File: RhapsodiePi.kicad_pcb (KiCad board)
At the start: 2 copper layers, 119 parts, among them J1 Micro_SD_Card_Det, J2 USB_A_Stacked, J3 USB_A_Stacked, J5 RJ45_HR913550A, U1 MT3420C-mt3420c, U1 X1000, U10 TPS65185RGZR, U2 MT3420C-mt3420c, U3 MT3420C-mt3420c, U5 AP6212, U6 FE2.1, U7 RTL8201F, U8 M25PX32-VMW, U9 TFP410PAP, X1 SG-3030CM

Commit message: Update (Display)
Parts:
- removed the U1 at (29.1, 35.7)
- removed the U1 at (111.4, 89.4)
- added C84: 22µ, Capacitor_SMD:C_0603_1608Metric, F.Cu at (43.2, 31.1)
- added C91: 4µ7, Capacitor_SMD:C_0805_2012Metric, F.Cu at (39.0, 33.5)
- added D10: LED, LED_SMD:LED_0402_1005Metric, F.Cu at (152.4, 76.2)
- added D12: LED, LED_SMD:LED_0402_1005Metric, F.Cu at (152.4, 78.6)
- added D13: LED, LED_SMD:LED_0402_1005Metric, F.Cu at (152.4, 81.0)
- added D4: LED, LED_SMD:LED_0402_1005Metric, F.Cu at (152.4, 69.0)
- added D6: LED, LED_SMD:LED_0402_1005Metric, F.Cu at (152.4, 71.4)
- added D8: LED, LED_SMD:LED_0402_1005Metric, F.Cu at (152.4, 73.8)
- added L4: 2µ2, Inductor_SMD:L_1008_2520Metric, F.Cu at (39.1, 25.6)
- added L5: 4µ7, Inductor_SMD:L_1008_2520Metric, F.Cu at (33.6, 30.9)
- added R1: 50K, Resistor_SMD:R_0402_1005Metric, F.Cu at (108.4, 34.2)
- added R14: 100K, Resistor_SMD:R_0402_1005Metric, F.Cu at (144.2, 40.4)
- added R17: 1K, Resistor_SMD:R_0402_1005Metric, F.Cu at (147.1, 38.4)
- added R18: 1K, Resistor_SMD:R_0402_1005Metric, F.Cu at (150.0, 38.4)
- added R19: 1K, Resistor_SMD:R_0402_1005Metric, F.Cu at (152.4, 67.8)
- added R2: 30K, Resistor_SMD:R_0402_1005Metric, F.Cu at (111.3, 36.2)
- added R20: 1K, Resistor_SMD:R_0402_1005Metric, F.Cu at (152.4, 70.2)
- added R21: 1K, Resistor_SMD:R_0402_1005Metric, F.Cu at (152.4, 72.6)
- added R22: 1K, Resistor_SMD:R_0402_1005Metric, F.Cu at (152.4, 75.0)
- added R23: 1K, Resistor_SMD:R_0402_1005Metric, F.Cu at (152.4, 77.4)
- added R24: 1K, Resistor_SMD:R_0402_1005Metric, F.Cu at (152.4, 79.8)
- added R26: 1K, Resistor_SMD:R_0402_1005Metric, F.Cu at (111.3, 41.7)
- added R27: 100K, Resistor_SMD:R_0402_1005Metric, F.Cu at (108.4, 43.7)
- added R28: 100K, Resistor_SMD:R_0402_1005Metric, F.Cu at (114.2, 43.7)
- added R29: 1K, Resistor_SMD:R_0402_1005Metric, F.Cu at (111.3, 43.7)
- added R3: 450K, Resistor_SMD:R_0402_1005Metric, F.Cu at (111.3, 32.2)
- added R30: 100K, Resistor_SMD:R_0402_1005Metric, F.Cu at (114.2, 41.7)
- added R31: 1K, Resistor_SMD:R_0402_1005Metric, F.Cu at (108.4, 41.7)
- added R32: 1K, Resistor_SMD:R_0402_1005Metric, F.Cu at (120.8, 41.7)
- added R33: 1K, Resistor_SMD:R_0402_1005Metric, F.Cu at (123.7, 41.7)
- added R4: 100K, Resistor_SMD:R_0402_1005Metric, F.Cu at (114.2, 36.2)
- added R5: 200K, Resistor_SMD:R_0402_1005Metric, F.Cu at (108.4, 36.2)
- added R6: 100K, Resistor_SMD:R_0402_1005Metric, F.Cu at (111.3, 34.2)
- added R7: 100K, Resistor_SMD:R_0402_1005Metric, F.Cu at (114.2, 34.2)
- added R8: 100K, Resistor_SMD:R_0402_1005Metric, F.Cu at (108.4, 32.2)
- added R9: 1K, Resistor_SMD:R_0402_1005Metric, F.Cu at (114.2, 32.2)
- added U1: MT3420C-mt3420c, Package_TO_SOT_SMD:SOT-23-6, F.Cu at (23.9, 51.3)
- added U4: X1000, TheBrutzlers_Lib:BGA256C80P16X16_1300X1300X130N, F.Cu at (121.8, 80.4)
- added Y1: 12MHz, Crystal:Crystal_SMD_ECS_CSM3X-2Pin_7.6x4.1mm, F.Cu at (145.2, 74.2)
- C47, C48: value C -> 20p
- C58, C67: value 1µ -> 100n
- C62: value C -> 1µ
- C65: value 100n -> C
- C69: value 100n -> 1µ
- C73: value 22µ -> 100n; footprint Capacitor_SMD:C_0603_1608Metric -> Capacitor_SMD:C_0402_1005Metric
- C74, C78, C85: value 4µ7 -> 22µ; footprint Capacitor_SMD:C_0805_2012Metric -> Capacitor_SMD:C_0603_1608Metric
- C75: value 22µ -> 4µ7; footprint Capacitor_SMD:C_0603_1608Metric -> Capacitor_SMD:C_0805_2012Metric
- C80, C86: value 100n -> 4µ7; footprint Capacitor_SMD:C_0402_1005Metric -> Capacitor_SMD:C_0805_2012Metric
- C81: value 10n -> 100n
- C83: value 4µ7 -> 10n; footprint Capacitor_SMD:C_0805_2012Metric -> Capacitor_SMD:C_0402_1005Metric
- C87: value 4µ7 -> 100n; footprint Capacitor_SMD:C_0805_2012Metric -> Capacitor_SMD:C_0402_1005Metric
- moved U7 103.7 mm to (59.6, 48.3), turned to 0 degrees
- moved C56 93.7 mm to (160.3, 53.2)
- moved C41 93.7 mm to (163.2, 53.2)
- moved C48 93.4 mm to (157.2, 55.2)
- moved C53 93.2 mm to (159.8, 57.2)
- moved C46 92.0 mm to (155.8, 59.1)
- moved C42 90.8 mm to (157.5, 53.2)
- moved C51 89.4 mm to (149.4, 46.3)
- moved C59 88.6 mm to (149.1, 48.2)
- moved C43 87.7 mm to (160.1, 55.2)
- moved C44 87.5 mm to (157.0, 57.2)
- moved C52 85.8 mm to (146.0, 50.2)
- moved C61 83.7 mm to (155.8, 61.1)
- moved C54 83.0 mm to (146.5, 46.3)
- moved C57 82.3 mm to (143.1, 52.2)
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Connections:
- AE1 pad 2: AGND2 -> GND
- C1 pad 2: AGND2 -> GND
- C10 pad 2: AGND2 -> GND
- C11 pad 2: AGND2 -> GND
- C12 pad 2: AGND2 -> GND
- C13 pad 2: AGND2 -> GND
- C14 pad 2: AGND2 -> GND
- C15 pad 2: AGND2 -> GND
- C16 pad 2: AGND2 -> GND
- C17 pad 2: AGND2 -> GND
- C18 pad 2: AGND2 -> GND
- C19 pad 2: AGND2 -> GND
- C2 pad 2: AGND2 -> GND
- C20 pad 2: AGND2 -> GND
- C21 pad 2: AGND2 -> GND
- C22 pad 2: AGND2 -> GND
- C23 pad 2: AGND2 -> GND
- C24 pad 2: AGND2 -> GND
- C25 pad 2: AGND2 -> GND
- C26 pad 2: AGND2 -> GND
- C27 pad 2: AGND2 -> GND
- C28 pad 2: AGND2 -> GND
- C29 pad 2: AGND2 -> GND
- C3 pad 2: AGND2 -> GND
- C30 pad 2: AGND2 -> GND
- C31 pad 2: AGND2 -> GND
- C32 pad 2: AGND2 -> GND
- C33 pad 2: AGND2 -> GND
- C34 pad 2: AGND2 -> GND
- C35 pad 2: AGND2 -> GND
- C36 pad 2: AGND2 -> GND
- C37 pad 2: AGND2 -> GND
- C38 pad 2: AGND2 -> GND
- C39 pad 2: AGND2 -> GND
- C4 pad 2: AGND2 -> GND
- C40 pad 2: AGND2 -> GND
- C41 pad 2: AGND2 -> GND
- C42 pad 2: AGND2 -> GND
- C43 pad 2: AGND2 -> GND
- C44 pad 2: AGND2 -> GND
- C45 pad 2: AGND2 -> GND
- C46 pad 2: AGND2 -> GND
- C47 pad 1: AGND2 -> GND
- C48 pad 1: AGND2 -> GND
- C49 pad 2: AGND2 -> GND
- C5 pad 2: AGND2 -> GND
- C50 pad 2: AGND2 -> GND
- C51 pad 2: AGND2 -> GND
- C52 pad 2: AGND2 -> GND
- C53 pad 2: AGND2 -> GND
- C54 pad 2: AGND2 -> GND
- C55 pad 1: Net-(C44-Pad1) -> GND
- C55 pad 2: AGND2 -> Net-(C55-Pad2)
- C56 pad 1: Net-(C50-Pad1) -> Net-(C44-Pad1)
- C56 pad 2: AGND2 -> GND
- C57 pad 1: Net-(C44-Pad1) -> Net-(C50-Pad1)
- C57 pad 2: AGND2 -> GND
- C58 pad 1: +5V -> Net-(C44-Pad1)
- C58 pad 2: AGND2 -> GND
- C59 pad 2: AGND2 -> GND
- C6 pad 2: AGND2 -> GND
- C60 pad 2: AGND2 -> GND
- C61 pad 2: AGND2 -> GND
- C62 pad 1: AGND2 -> +5V
- C62 pad 2: Net-(C62-Pad2) -> GND
- C63 pad 1: AGND2 -> GND
- C64 pad 1: AGND2 -> GND
- C65 pad 1: Net-(C65-Pad1) -> GND
- C65 pad 2: AGND2 -> Net-(C65-Pad2)
- C66 pad 2: AGND2 -> GND
- C67 pad 1: AGND2 -> Net-(C67-Pad1)
- C67 pad 2: +3V3 -> GND
- C68 pad 1: AGND2 -> GND
- C68 pad 2: Net-(C68-Pad2) -> +3V3
- C69 pad 1: AGND2 -> GND
- C69 pad 2: +3V3 -> Net-(C69-Pad2)
- C7 pad 2: AGND2 -> GND
- C70 pad 1: AGND2 -> GND
- C70 pad 2: Net-(C68-Pad2) -> +3V3
- C71 pad 1: AGND2 -> GND
- C71 pad 2: Net-(C71-Pad2) -> Net-(C69-Pad2)
- C72 pad 1: AGND2 -> GND
- C73 pad 1: unconnected-(C73-Pad1) -> GND
- C73 pad 2: unconnected-(C73-Pad2) -> Net-(C73-Pad2)
- C74 pad 1: AGND2 -> unconnected-(C74-Pad1)
- C74 pad 2: /Display/E-PAPER/VB -> unconnected-(C74-Pad2)
- C75 pad 1: AGND2 -> GND
- C75 pad 2: +5V -> /Display/E-PAPER/VB
- C76 pad 1: +5V -> GND
- C76 pad 2: AGND2 -> +5V
- C77 pad 2: AGND2 -> GND
- C78 pad 1: AGND2 -> +5V
- C78 pad 2: /Display/E-PAPER/VN -> GND
- C79 pad 1: /Display/E-PAPER/VB -> GND
- C79 pad 2: AGND2 -> /Display/E-PAPER/VN
- C8 pad 2: AGND2 -> GND
- C80 pad 1: Net-(C80-Pad1) -> /Display/E-PAPER/VB
- C80 pad 2: AGND2 -> GND
- C81 pad 2: Net-(C81-Pad2) -> GND
- C83 pad 1: AGND2 -> Net-(C83-Pad1)
- C85 pad 1: AGND2 -> Net-(C85-Pad1)
- C85 pad 2: Net-(C85-Pad2) -> GND
- C86 pad 1: Net-(C86-Pad1) -> GND
- C86 pad 2: AGND2 -> Net-(C86-Pad2)
- C87 pad 1: AGND2 -> Net-(C87-Pad1)
- C87 pad 2: Net-(C87-Pad2) -> GND
- C88 pad 1: AGND2 -> GND
- C88 pad 2: /Display/E-PAPER/VEE -> Net-(C88-Pad2)
- C89 pad 1: AGND2 -> GND
- C89 pad 2: /Display/E-PAPER/VDDH -> /Display/E-PAPER/VEE
- C9 pad 2: AGND2 -> GND
- C90 pad 1: /Display/E-PAPER/VN -> GND
- C90 pad 2: AGND2 -> /Display/E-PAPER/VDDH
- D15 pad 1: Net-(C80-Pad1) -> Net-(C81-Pad1)
- D15 pad 2: Net-(C81-Pad2) -> Net-(C82-Pad2)
- D16 pad 1: Net-(C82-Pad2) -> Net-(C83-Pad2)
- D16 pad 2: Net-(C86-Pad1) -> Net-(C87-Pad1)
- D17 pad 1: Net-(C81-Pad2) -> Net-(C82-Pad2)
- D18 pad 2: Net-(C82-Pad2) -> Net-(C83-Pad2)
- FB1 pad 2: Net-(C68-Pad2) -> Net-(C69-Pad2)
- J1 pad 10: AGND2 -> GND
- J1 pad 6: AGND2 -> GND
- J2 pad 4: AGND2 -> GND
- J2 pad 8: AGND2 -> GND
- J2 pad 9: AGND2 -> GND
- J3 pad 4: AGND2 -> GND
- J3 pad 8: AGND2 -> GND
- J3 pad 9: AGND2 -> GND
- J5 pad 2: Net-(C65-Pad1) -> Net-(C66-Pad1)
- J5 pad 5: Net-(C66-Pad1) -> Net-(C67-Pad1)
- J5 pad 8: AGND2 -> GND
- J5 pad SH: AGND2 -> GND
- R13 pad 2: AGND2 -> GND
- R16 pad 1: AGND2 -> GND
- U10 pad 1: Net-(C84-Pad1) -> Net-(C85-Pad1)
- U10 pad 12: unconnected-(U10-Pad12) -> /Display/E-PAPER/XVCOM_CTRL
- U10 pad 15: Net-(C83-Pad2) -> /Display/E-PAPER/VCOM
- U10 pad 17: unconnected-(U10-Pad17) -> /Display/E-PAPER/XSCL
- U10 pad 18: unconnected-(U10-Pad18) -> /Display/E-PAPER/XSDA
- U10 pad 2: unconnected-(U10-Pad2) -> /Display/E-PAPER/X~{INT}
- U10 pad 21: unconnected-(U10-Pad21) -> /Display/E-PAPER/XPWRUP
- U10 pad 23: unconnected-(U10-Pad23) -> /Display/E-PAPER/XPWR_GOOD
- U10 pad 28: Net-(C81-Pad1) -> Net-(C82-Pad1)
- U10 pad 3: Net-(C85-Pad2) -> Net-(C86-Pad2)
- U10 pad 30: Net-(C80-Pad1) -> Net-(C81-Pad1)
- U10 pad 32: AGND2 -> GND
- U10 pad 34: Net-(C86-Pad1) -> Net-(C87-Pad1)
- U10 pad 36: Net-(C82-Pad1) -> Net-(C83-Pad1)
- U10 pad 41: AGND2 -> GND
- U10 pad 44: Net-(C87-Pad2) -> Net-(C88-Pad2)
- U10 pad 46: unconnected-(U10-Pad46) -> /Display/E-PAPER/VDD
- U10 pad 48: AGND2 -> GND
- U10 pad 5: unconnected-(U10-Pad5) -> /Display/E-PAPER/XWAKEU
- U10 pad 6: AGND2 -> GND
- U10 pad 8: AGND2 -> GND
- U2 pad 2: AGND2 -> GND
- U3 pad 2: AGND2 -> GND
- U5 pad 1: AGND2 -> GND
- U5 pad 20: AGND2 -> GND
- U5 pad 3: AGND2 -> GND
- U5 pad 31: AGND2 -> GND
- U5 pad 33: AGND2 -> GND
- U5 pad 36: AGND2 -> GND
- U6 pad 10: AGND2 -> GND
- U6 pad 24: AGND2 -> GND
- U6 pad 39: AGND2 -> GND
- U6 pad 40: Net-(R15-Pad2) -> Net-(C55-Pad2)
- U7 pad 2: Net-(C72-Pad2) -> Net-(C73-Pad2)
- U7 pad 29: Net-(C71-Pad2) -> Net-(C72-Pad2)
- U7 pad 30: Net-(C68-Pad2) -> Net-(C69-Pad2)
- U7 pad 33: AGND2 -> GND
- U7 pad 7: Net-(C68-Pad2) -> Net-(C69-Pad2)
- U8 pad 4: AGND2 -> GND
- X1 pad 2: AGND2 -> GND

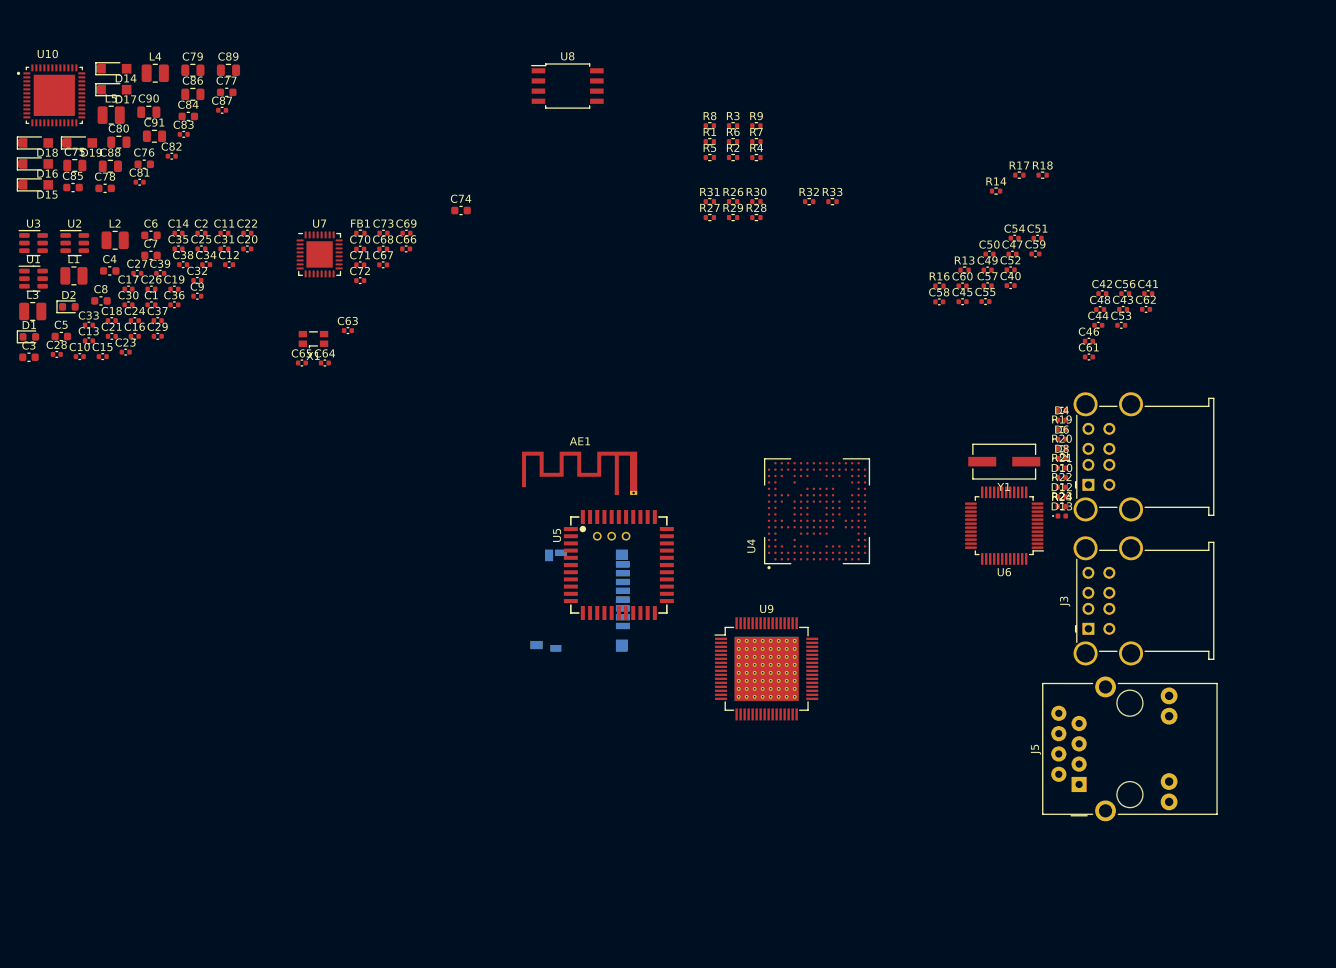
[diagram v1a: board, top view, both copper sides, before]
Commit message: Add Audio
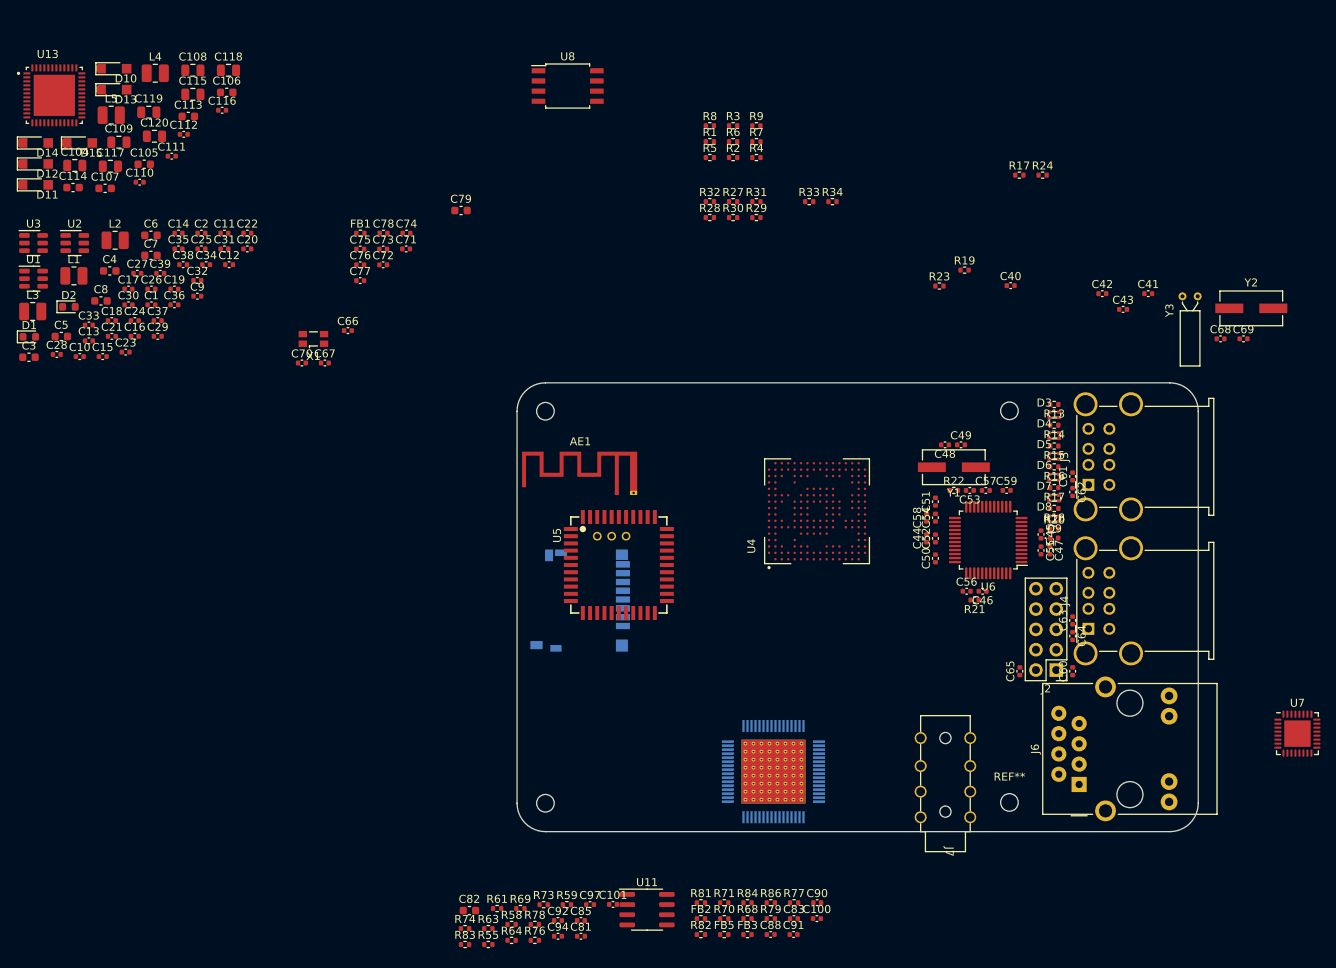
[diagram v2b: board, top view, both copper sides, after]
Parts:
- removed the D10 at (152.4, 76.2)
- removed the D12 at (152.4, 78.6)
- removed the D13 at (152.4, 81.0)
- added ?: , , F.Cu at (87.8, 116.9)
- added ?: , , F.Cu at (145.8, 67.8)
- added ?: , , F.Cu at (87.8, 67.9)
- added C100: 1µ, Capacitor_SMD:C_0402_1005Metric, F.Cu at (121.8, 131.3)
- added C101: 1µ, Capacitor_SMD:C_0402_1005Metric, F.Cu at (96.3, 129.6)
- added C58: 100n, Capacitor_SMD:C_0402_1005Metric, F.Cu at (135.5, 81.2)
- added C60: 1µ, Capacitor_SMD:C_0402_1005Metric, F.Cu at (153.8, 100.4)
- added C65: 1µ, Capacitor_SMD:C_0402_1005Metric, F.Cu at (147.2, 100.4)
- added C68: C, Capacitor_SMD:C_0402_1005Metric, F.Cu at (172.2, 58.9)
- added C69: C, Capacitor_SMD:C_0402_1005Metric, F.Cu at (175.1, 58.9)
- added C81: 100n, Capacitor_SMD:C_0402_1005Metric, F.Cu at (92.3, 133.5)
- added C82: 22µ, Capacitor_SMD:C_0603_1608Metric, F.Cu at (78.3, 130.3)
- added C83: 1n, Capacitor_SMD:C_0402_1005Metric, F.Cu at (118.9, 131.3)
- added C85: 1µ, Capacitor_SMD:C_0402_1005Metric, F.Cu at (92.3, 131.6)
- added C88: 220p, Capacitor_SMD:C_0402_1005Metric, F.Cu at (116.0, 133.3)
- added C90: 220p, Capacitor_SMD:C_0402_1005Metric, F.Cu at (121.8, 129.3)
- added C91: 220p, Capacitor_SMD:C_0402_1005Metric, F.Cu at (118.9, 133.3)
- added C92: 220p, Capacitor_SMD:C_0402_1005Metric, F.Cu at (89.4, 131.6)
- added C94: 1n, Capacitor_SMD:C_0402_1005Metric, F.Cu at (89.4, 133.5)
- added C97: 1n, Capacitor_SMD:C_0402_1005Metric, F.Cu at (93.4, 129.6)
- added D3: LED_Dual_LED, TheBrutzlers_Lib:DUAL_LED_0603, F.Cu at (151.4, 68.3)
- added D5: LED_Dual_LED, TheBrutzlers_Lib:DUAL_LED_0603, F.Cu at (151.4, 73.5)
- added D7: LED_Dual_LED, TheBrutzlers_Lib:DUAL_LED_0603, F.Cu at (151.4, 78.8)
- added D9: LED, LED_SMD:LED_0402_1005Metric, F.Cu at (151.4, 83.8)
- added FB2: FerriteBead, Resistor_SMD:R_0402_1005Metric, F.Cu at (107.3, 131.3)
- added FB3: FerriteBead, Resistor_SMD:R_0402_1005Metric, F.Cu at (113.1, 133.3)
- added FB5: FerriteBead, Resistor_SMD:R_0402_1005Metric, F.Cu at (110.2, 133.3)
- added J2: Conn_02x05_Odd_Even, Connector_PinHeader_2.54mm:PinHeader_2x05_P2.54mm_Vertical, F.Cu at (151.7, 100.2)
- added J7: AudioJack4, TheBrutzlers_Lib:AUDIO_3.5mm_PJ-313B6-B, F.Cu at (137.8, 123.0)
- added R18: 1K, Resistor_SMD:R_0402_1005Metric, F.Cu at (151.4, 80.0)
- added R22: 1MEG, Resistor_SMD:R_0402_1005Metric, F.Cu at (138.9, 77.8)
- added R55: 2K2, Resistor_SMD:R_0402_1005Metric, F.Cu at (80.7, 134.6)
- added R58: 2K7, Resistor_SMD:R_0402_1005Metric, F.Cu at (83.6, 132.1)
- added R59: 2K7, Resistor_SMD:R_0402_1005Metric, F.Cu at (90.5, 129.6)
- added R61: 2K7, Resistor_SMD:R_0402_1005Metric, F.Cu at (81.8, 130.1)
- added R63: 2K7, Resistor_SMD:R_0402_1005Metric, F.Cu at (80.7, 132.6)
- added R64: 2K7, Resistor_SMD:R_0402_1005Metric, F.Cu at (83.6, 134.0)
- added R68: 2K7, Resistor_SMD:R_0402_1005Metric, F.Cu at (113.1, 131.3)
- added R69: 2K7, Resistor_SMD:R_0402_1005Metric, F.Cu at (84.7, 130.1)
- added R70: 2K7, Resistor_SMD:R_0402_1005Metric, F.Cu at (110.2, 131.3)
- added R71: 2K7, Resistor_SMD:R_0402_1005Metric, F.Cu at (110.2, 129.3)
- added R73: 10K, Resistor_SMD:R_0402_1005Metric, F.Cu at (87.6, 129.6)
- added R74: 10K, Resistor_SMD:R_0402_1005Metric, F.Cu at (77.8, 132.6)
- added R76: 10K, Resistor_SMD:R_0402_1005Metric, F.Cu at (86.5, 134.0)
- added R77: 20K, Resistor_SMD:R_0402_1005Metric, F.Cu at (118.9, 129.3)
- added R78: 20K, Resistor_SMD:R_0402_1005Metric, F.Cu at (86.5, 132.1)
- added R79: 20K, Resistor_SMD:R_0402_1005Metric, F.Cu at (116.0, 131.3)
- added R81: 10K, Resistor_SMD:R_0402_1005Metric, F.Cu at (107.3, 129.3)
- added R82: 10K, Resistor_SMD:R_0402_1005Metric, F.Cu at (107.3, 133.3)
- added R83: 0R, Resistor_SMD:R_0402_1005Metric, F.Cu at (77.8, 134.6)
- added R84: 0R, Resistor_SMD:R_0402_1005Metric, F.Cu at (113.1, 129.3)
- added R86: 0R, Resistor_SMD:R_0402_1005Metric, F.Cu at (116.0, 129.3)
- added REF**: MountingHole_2.2mm_M2, MountingHole:MountingHole_2.2mm_M2, F.Cu at (145.8, 116.8)
- added U11: LM4871, Package_SO:SOIC-8_3.9x4.9mm_P1.27mm, F.Cu at (100.5, 130.2)
- added Y2: 24MHz, Crystal:Crystal_SMD_ECS_CSM3X-2Pin_7.6x4.1mm, F.Cu at (176.1, 55.0)
- added Y3: 32.768kHz, Crystal:Crystal_C26-LF_D2.1mm_L6.5mm_Horizontal, F.Cu at (167.5, 53.5)
- D4, D6, D8: value LED -> LED_Dual_LED; footprint LED_SMD:LED_0402_1005Metric -> TheBrutzlers_Lib:DUAL_LED_0603
- U9: moved to B.Cu
- moved U7 136.1 mm to (181.8, 108.2)
- moved R21 51.2 mm to (141.5, 91.5), turned to 180 degrees
- moved C64 41.8 mm to (153.8, 96.0), turned to -90 degrees
- moved C52 39.6 mm to (136.6, 83.8), turned to 90 degrees
- moved C47 37.8 mm to (150.9, 85.3), turned to -90 degrees
- moved C50 36.6 mm to (136.6, 86.3), turned to 90 degrees
- moved C56 36.3 mm to (140.5, 90.4)
- moved C44 34.2 mm to (135.5, 83.8), turned to 90 degrees
- moved C46 34.0 mm to (142.5, 90.4), turned to 180 degrees
- moved C55 33.7 mm to (149.8, 85.3), turned to -90 degrees
- moved C54 33.4 mm to (136.6, 81.2), turned to 90 degrees
- moved C63 33.0 mm to (153.8, 94.0), turned to 90 degrees
- moved C53 32.0 mm to (140.9, 77.8), turned to 180 degrees
- moved C45 30.7 mm to (149.8, 83.3), turned to -90 degrees
- moved C51 30.5 mm to (136.6, 79.2), turned to 90 degrees
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- renumbered C75 to C104, C76 to C105, C77 to C106, C78 to C107, C79 to C108, C80 to C109, C81 to C110, C82 to C111, C83 to C112, C84 to C113, C85 to C114, C86 to C115, C87 to C116, C88 to C117, C89 to C118, C90 to C119, C91 to C120, C50 to C47, C47 to C48, C48 to C49, C49 to C50, C52 to C51, C51 to C52, C54 to C53, C53 to C54, C57 to C55, C55 to C56, C56 to C57, C58 to C59, C59 to C61, C60 to C62, C61 to C63, C62 to C64, C63 to C66, C64 to C67, C65 to C70, C66 to C71, C67 to C72, C68 to C73, C69 to C74, C70 to C75, C71 to C76, C72 to C77, C73 to C78, C74 to C79, D14 to D10, D15 to D11, D16 to D12, D17 to D13, D18 to D14, D19 to D15, J2 to J3, J3 to J4, J5 to J6, R19 to R13, R20 to R14, R21 to R15, R22 to R16, R23 to R17, R13 to R19, R24 to R20, R14 to R21, R16 to R23, R18 to R24, R26 to R27, R27 to R28, R28 to R29, R29 to R30, R30 to R31, R31 to R32, R32 to R33, R33 to R34, U10 to U13
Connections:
- AE1 pad 2: GND -> AGND2
- C1 pad 2: GND -> AGND2
- C10 pad 2: GND -> AGND2
- C104 pad 1: GND -> AGND2
- C105 pad 1: GND -> AGND2
- C106 pad 2: GND -> AGND2
- C107 pad 2: GND -> AGND2
- C108 pad 1: GND -> AGND2
- C109 pad 2: GND -> AGND2
- C11 pad 2: GND -> AGND2
- C110 pad 2: GND -> AGND2
- C113 pad 2: GND -> AGND2
- C114 pad 2: GND -> AGND2
- C115 pad 1: GND -> AGND2
- C116 pad 2: GND -> AGND2
- C117 pad 1: GND -> AGND2
- C118 pad 1: GND -> AGND2
- C119 pad 1: GND -> AGND2
- C12 pad 2: GND -> AGND2
- C120 pad 2: GND -> AGND2
- C13 pad 2: GND -> AGND2
- C14 pad 2: GND -> AGND2
- C15 pad 2: GND -> AGND2
- C16 pad 2: GND -> AGND2
- C17 pad 2: GND -> AGND2
- C18 pad 2: GND -> AGND2
- C19 pad 2: GND -> AGND2
- C2 pad 2: GND -> AGND2
- C20 pad 2: GND -> AGND2
- C21 pad 2: GND -> AGND2
- C22 pad 2: GND -> AGND2
- C23 pad 2: GND -> AGND2
- C24 pad 2: GND -> AGND2
- C25 pad 2: GND -> AGND2
- C26 pad 2: GND -> AGND2
- C27 pad 2: GND -> AGND2
- C28 pad 2: GND -> AGND2
- C29 pad 2: GND -> AGND2
- C3 pad 2: GND -> AGND2
- C30 pad 2: GND -> AGND2
- C31 pad 2: GND -> AGND2
- C32 pad 2: GND -> AGND2
- C33 pad 2: GND -> AGND2
- C34 pad 2: GND -> AGND2
- C35 pad 2: GND -> AGND2
- C36 pad 2: GND -> AGND2
- C37 pad 2: GND -> AGND2
- C38 pad 2: GND -> AGND2
- C39 pad 2: GND -> AGND2
- C4 pad 2: GND -> AGND2
- C40 pad 2: GND -> AGND2
- C41 pad 2: GND -> AGND2
- C42 pad 2: GND -> AGND2
- C43 pad 2: GND -> AGND2
- C44 pad 2: GND -> AGND2
- C45 pad 2: GND -> AGND2
- C46 pad 2: GND -> AGND2
- C47 pad 2: GND -> AGND2
- C48 pad 1: GND -> AGND2
- C49 pad 1: GND -> AGND2
- C5 pad 2: GND -> AGND2
- C50 pad 2: GND -> AGND2
- C51 pad 2: GND -> AGND2
- C52 pad 2: GND -> AGND2
- C53 pad 2: GND -> AGND2
- C54 pad 2: GND -> AGND2
- C55 pad 2: GND -> AGND2
- C56 pad 1: GND -> AGND2
- C57 pad 2: GND -> AGND2
- C59 pad 2: GND -> AGND2
- C6 pad 2: GND -> AGND2
- C61 pad 2: GND -> AGND2
- C62 pad 2: GND -> AGND2
- C63 pad 2: GND -> AGND2
- C64 pad 2: GND -> AGND2
- C66 pad 1: GND -> AGND2
- C67 pad 1: GND -> AGND2
- C7 pad 2: GND -> AGND2
- C70 pad 1: GND -> AGND2
- C71 pad 2: GND -> AGND2
- C72 pad 2: GND -> AGND2
- C73 pad 1: GND -> AGND2
- C74 pad 1: GND -> AGND2
- C75 pad 1: GND -> AGND2
- C76 pad 1: GND -> AGND2
- C77 pad 1: GND -> AGND2
- C78 pad 1: GND -> AGND2
- C8 pad 2: GND -> AGND2
- C9 pad 2: GND -> AGND2
- D4 pad 1: DRV -> Net-(D4-Pad1)
- D4 pad 2: Net-(D4-Pad2) -> DRV
- D6 pad 1: DRV -> Net-(D6-Pad1)
- D6 pad 2: Net-(D6-Pad2) -> DRV
- D8 pad 1: DRV -> Net-(D8-Pad1)
- D8 pad 2: Net-(D8-Pad2) -> DRV
- J1 pad 10: GND -> AGND2
- J1 pad 6: GND -> AGND2
- J3 pad 4: GND -> AGND2
- J3 pad 8: GND -> AGND2
- J3 pad 9: GND -> AGND2
- J4 pad 4: GND -> AGND2
- J4 pad 8: GND -> AGND2
- J4 pad 9: GND -> AGND2
- J6 pad 8: GND -> AGND2
- J6 pad SH: GND -> AGND2
- L5 pad 2: GND -> AGND2
- R13 pad 1: Net-(D4-Pad2) -> Net-(D3-Pad1)
- R14 pad 1: Net-(D6-Pad2) -> Net-(D4-Pad1)
- R15 pad 1: Net-(D8-Pad2) -> Net-(D5-Pad1)
- R16 pad 1: Net-(D10-Pad2) (its old number) -> Net-(D6-Pad1)
- R19 pad 2: GND -> AGND2
- R23 pad 1: GND -> AGND2
- R24 pad 2: GND -> AGND2
- R28 pad 2: GND -> AGND2
- R30 pad 2: GND -> AGND2
- R32 pad 2: GND -> AGND2
- R34 pad 1: GND -> AGND2
- R4 pad 2: GND -> AGND2
- R6 pad 2: GND -> AGND2
- R8 pad 2: GND -> AGND2
- U1 pad 2: GND -> AGND2
- U13 pad 32: GND -> AGND2
- U13 pad 41: GND -> AGND2
- U13 pad 48: GND -> AGND2
- U13 pad 6: GND -> AGND2
- U13 pad 8: GND -> AGND2
- U2 pad 2: GND -> AGND2
- U3 pad 2: GND -> AGND2
- U4 pad A8: GND -> AGND2
- U4 pad E10: GND -> AGND2
- U4 pad E9: GND -> AGND2
- U4 pad F10: GND -> AGND2
- U4 pad F9: GND -> AGND2
- U4 pad G10: GND -> AGND2
- U4 pad G9: GND -> AGND2
- U4 pad J10: GND -> AGND2
- U4 pad J5: GND -> AGND2
- U4 pad J6: GND -> AGND2
- U4 pad J7: GND -> AGND2
- U4 pad K10: GND -> AGND2
- U4 pad K5: GND -> AGND2
- U4 pad K6: GND -> AGND2
- U4 pad K7: GND -> AGND2
- U4 pad K8: GND -> AGND2
- U4 pad K9: GND -> AGND2
- U4 pad L10: GND -> AGND2
- U4 pad L11: GND -> AGND2
- U4 pad L6: GND -> AGND2
- U4 pad L7: GND -> AGND2
- U4 pad L8: GND -> AGND2
- U4 pad L9: GND -> AGND2
- U4 pad M10: GND -> AGND2
- U4 pad M14: GND -> AGND2
- U4 pad M15: unconnected-(U4-PadM15) -> Net-(C86-Pad1)
- U4 pad M16: unconnected-(U4-PadM16) -> Net-(C87-Pad1)
- U4 pad M8: GND -> AGND2
- U4 pad M9: GND -> AGND2
- U4 pad N15: unconnected-(U4-PadN15) -> Net-(C84-Pad1)
- U4 pad N16: unconnected-(U4-PadN16) -> Net-(C85-Pad1)
- U4 pad N7: GND -> AGND2
- U4 pad P10: GND -> AGND2
- U4 pad P14: GND -> AGND2
- U4 pad P15: unconnected-(U4-PadP15) -> Net-(C79-Pad2)
- U4 pad P9: GND -> AGND2
- U4 pad R11: GND -> AGND2
- U4 pad R14: unconnected-(U4-PadR14) -> Net-(C83-Pad1)
- U4 pad R15: unconnected-(U4-PadR15) -> Net-(R56-Pad1)
- U4 pad R16: unconnected-(U4-PadR16) -> Net-(R55-Pad1)
- U4 pad R8: Net-(U4-PadR8) -> Net-(C68-Pad2)
- U4 pad T15: unconnected-(U4-PadT15) -> Net-(C81-Pad2)
- U4 pad T8: unconnected-(U4-PadT8) -> Net-(C69-Pad2)
- U5 pad 1: GND -> AGND2
- U5 pad 20: GND -> AGND2
- U5 pad 3: GND -> AGND2
- U5 pad 31: GND -> AGND2
- U5 pad 33: GND -> AGND2
- U5 pad 36: GND -> AGND2
- U6 pad 10: GND -> AGND2
- U6 pad 24: GND -> AGND2
- U6 pad 32: unconnected-(U6-Pad32) -> DP5-
- U6 pad 33: unconnected-(U6-Pad33) -> DP5+
- U6 pad 34: unconnected-(U6-Pad34) -> DP6-
- U6 pad 35: unconnected-(U6-Pad35) -> DP6+
- U6 pad 39: GND -> AGND2
- U6 pad 47: Net-(R17-Pad1) -> LED6
- U7 pad 33: GND -> AGND2
- U8 pad 4: GND -> AGND2
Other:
- board outline added: 85.2 x 56.1 mm

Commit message: New i.mx6 Version
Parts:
- moved U4 2.44 mm to (123.5, 82.1)
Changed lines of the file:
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@@
   )
   (footprint "TheBrutzlers_Lib:BGA256C80P16X16_1300X1300X130N" (layer "F.Cu")
-    (at 121.8 80.4 90)
+    (at 123.55 82.1 90)
     (property "Sheetfile" "PowerSupply.kicad_sch")
     (property "Sheetname" "PowerSupply")
